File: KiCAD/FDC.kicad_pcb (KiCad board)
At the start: 2 copper layers, 53.5 x 110.5 mm, 28 parts, among them J1 Conn_01x01_Pin, Q1 FDV301N, Q2 FDV301N, U1 Z80, U2 Z80, U23 SN74LS32NSR, U3 SN74LVCC4245APWR, U4 SN74LVC245APWR, U5 SN74LVC245APWR, U6 SN74LVC245APWR, U7 SN74LVC245APWR

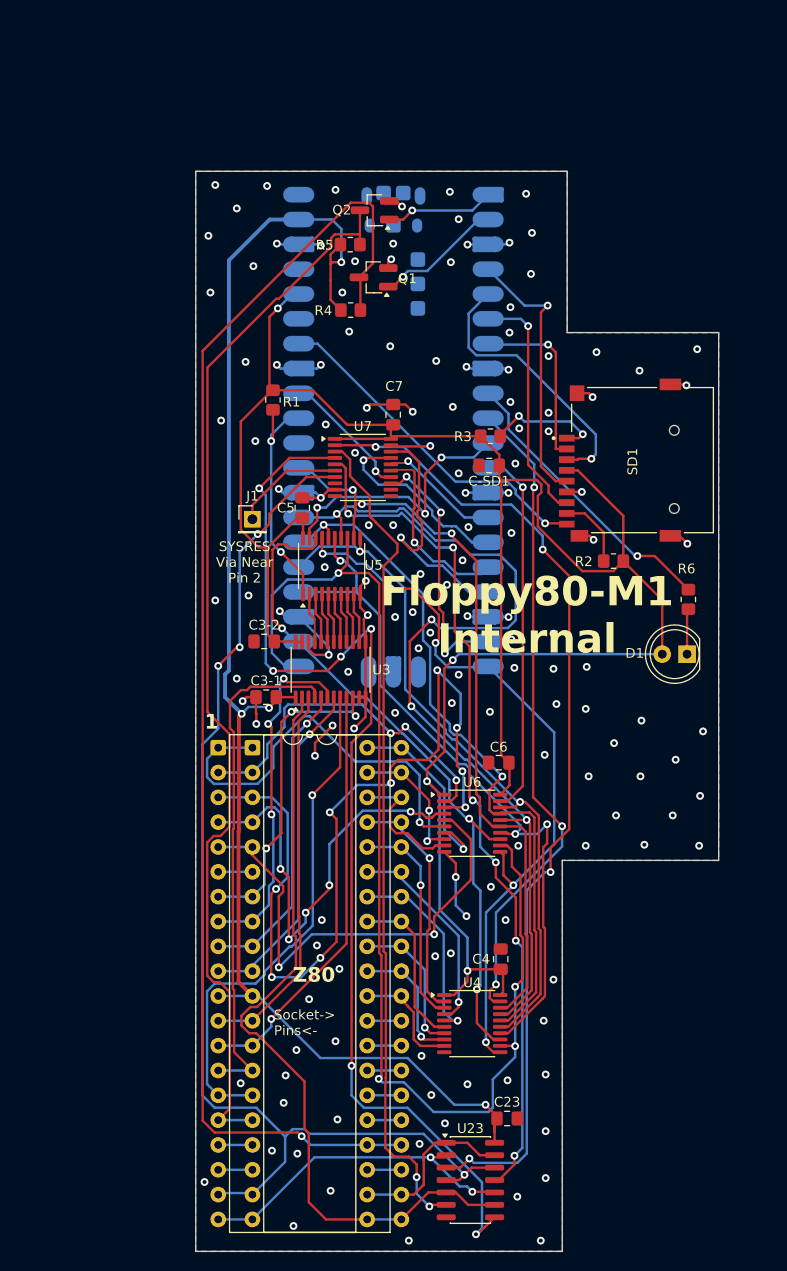
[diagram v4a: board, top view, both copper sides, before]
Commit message: Dropped additional level shifter/corrected soic size.
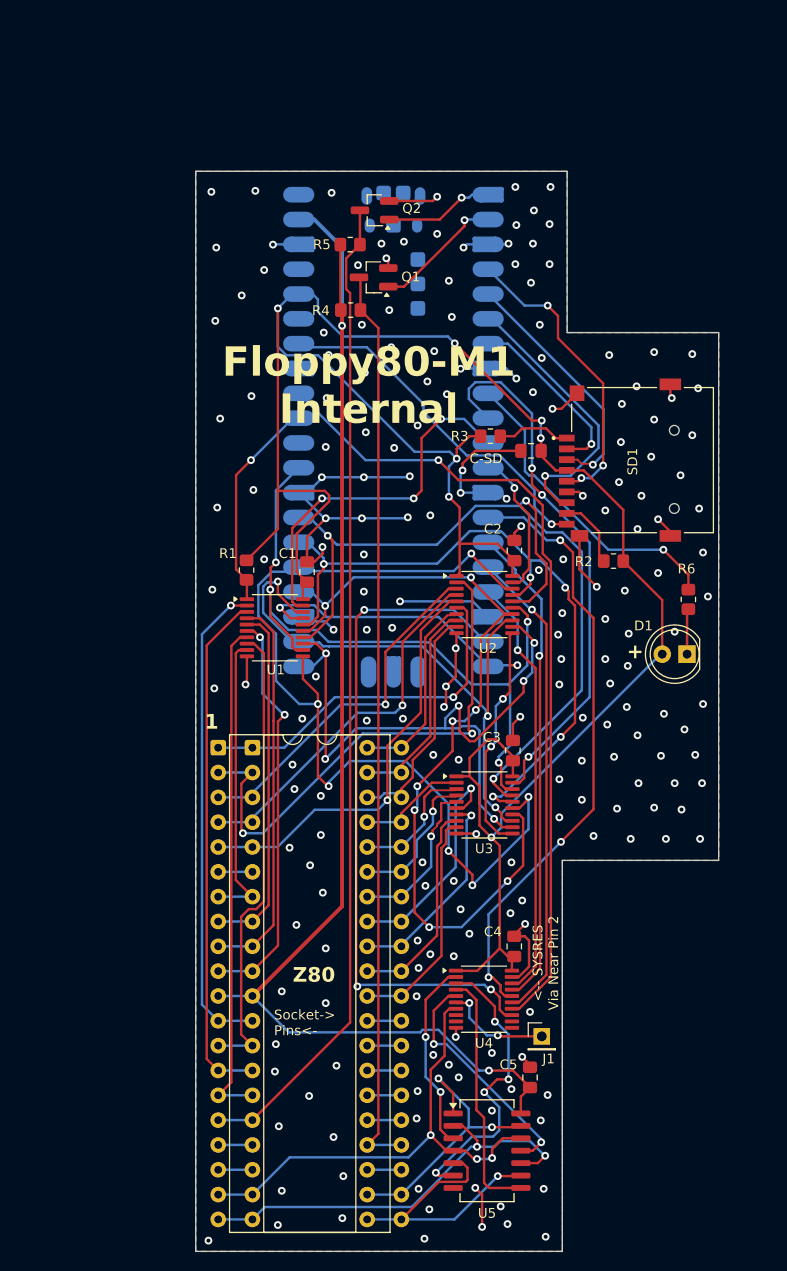
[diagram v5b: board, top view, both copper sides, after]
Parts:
- removed C3-1, C3-2: 100nF, Capacitor_SMD:C_0805_2012Metric_Pad1.18x1.45mm_HandSolder
- removed U23: SN74LS32NSR, Package_SO:SOIC-14_3.9x8.7mm_P1.27mm
- removed the U3 at (140.3, 89.5)
- added U5: SN74LS32NSR, Package_SO:SO-14_5.3x10.2mm_P1.27mm, F.Cu at (156.3, 138.7)
- moved J1 60.6 mm to (161.9, 127.0)
- moved U4 55.8 mm to (156.0, 123.2)
- moved C4 55.8 mm to (159.1, 117.8)
- moved U2 22.4 mm to (156.0, 82.8)
- moved U3 22.4 mm to (156.0, 103.3)
- moved C2 21.8 mm to (159.1, 77.3), turned to 90 degrees
- moved C3 21.4 mm to (158.9, 97.8)
- moved R1 17.6 mm to (131.7, 79.3)
- moved U1 8.57 mm to (134.6, 85.2), turned to 0 degrees
- moved C1 6.58 mm to (137.9, 79.5)
- moved C5 4.81 mm to (160.7, 131.2), turned to 90 degrees
- moved C-SD 4.53 mm to (160.8, 67.1)
- renumbered C-SD1 to C-SD, C5 to C1, C6 to C2, C4 to C3, C7 to C4, C23 to C5, U5 to U1, U1 to U10, U2 to U11, U6 to U2, U4 to U3, U7 to U4
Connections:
- U1 pad 2: /D2- -> /D2
- U1 pad 3: /D0- -> /D0
- U1 pad 4: /D5- -> /D5
- U1 pad 5: /D3- -> /D3
- U1 pad 6: /D6- -> /D6
- U1 pad 7: /D1- -> /D1
- U1 pad 8: /D7- -> /D7
- U1 pad 9: /D4- -> /D4
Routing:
- net /IN5V: track 114.0 -> 25.5 mm, vias 6 -> 0
- net /OUT5V: track 100.7 -> 19.7 mm, vias 4 -> 2
- net /SYSRES': track 13.6 -> 83.6 mm
- net /MREQ: track 118.4 -> 50.3 mm, vias 4 -> 3
- net /WR5V: track 87.9 -> 24.1 mm, vias 6 -> 2
- net /RD5V: track 85.8 -> 30.8 mm, vias 2 -> 4
- net /D1': track 120.7 -> 69.3 mm, vias 4 -> 6
- net /A13: track 87.6 -> 36.6 mm, vias 9 -> 1
- net /RD*: track 79.5 -> 28.9 mm, vias 0 -> 1
- net /IN': track 12.6 -> 62.5 mm, vias 1 -> 3
- net /MREQ': track 26.7 -> 71.3 mm
- net /WAIT*: track 135.2 -> 93.6 mm, vias 1 -> 0
- net /WR': track 19.1 -> 49.0 mm
- net /RD': track 20.0 -> 49.8 mm
- net GND: track 102.3 -> 130.9 mm, vias 147 -> 203
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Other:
- board text added: "+"
- board text added: "<-- SYSRES Via Near Pin 2"
- board text added: "All Caps - 100NF R1,R2,R3,R4,R5 - 1k R6 - 100 OHM U1,U2,U3,U4 - SN74LVC245APWR U5 - SN74LS32NSR SD - MSD-1-A Q1,Q2 - FDV301N"
- board text added: "Floppy80-M1 ver 1.3 Internal version by dabone (2026) https://github.com/dabonetn/Floppy80-M1-Internal Original By MichaelM4 https://github.com/MichaelM4/Floppy80-M1"
- board text added: "Pico 2 (SC1631)"
- board text removed: "All Caps - 100NF R1,R2,R3,R4,R5 - 1k R6 - 100 OHM U3 - SN74LVCC4245APWR U4,U5,U6, U7 - SN74LVC245APWR U23 - SN74LS32NSR SD - MSD-1-A Q1,Q2 - FDV301N"
- board text removed: "Floppy80-M1 ver 1.21 Internal version by dabone (2026) https://github.com/dabonetn/Floppy80-M1-Internal Original By MichaelM4 https://github.com/MichaelM4/Floppy80-M1"
- board text removed: "SYSRES Via Near Pin 2"
